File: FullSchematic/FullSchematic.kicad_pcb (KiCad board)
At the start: 4 copper layers, 106 parts, among them J1 USB_A, J10 LCD_Conn, J2 ATX-24, J3 Red Banana Jack, J4 Black Banana Jack, J5 2x6 Pin Header, J6 2x6 Pin Header, J7 CT3151-2, J8 CT3151-2, J9 2x6 Pin Header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

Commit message: Lots of changes with greg
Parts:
- C29, C36, C37, D3, Q3, R21, R22, U10, U11, U12, U13, U14, U9: moved to B.Cu
- moved R15 164.0 mm to (187.5, 70.4)
- moved R19 158.3 mm to (180.7, 68.9)
- moved U8 152.8 mm to (192.8, 79.9)
- moved R16 146.6 mm to (187.5, 65.9)
- moved R20 143.6 mm to (182.8, 65.0)
- moved TP8 138.8 mm to (165.7, 30.1), turned to 90 degrees
- moved TP7 134.1 mm to (162.4, 30.1), turned to 90 degrees
- moved TP6 129.4 mm to (159.0, 30.1), turned to 90 degrees
- moved TP5 124.7 mm to (155.7, 30.1), turned to 90 degrees
- moved TP4 120.0 mm to (152.3, 30.1), turned to 90 degrees
- moved C28 120.0 mm to (98.0, 152.7)
- moved C35 115.5 mm to (98.0, 148.0), turned to 180 degrees
- moved U11 110.4 mm to (106.1, 149.1), turned to 180 degrees
- moved U10 110.0 mm to (106.2, 144.2), turned to 180 degrees
- moved C29 106.9 mm to (82.6, 150.7), turned to 180 degrees
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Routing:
- net COM: track 15.6 -> 154.7 mm, vias 9 -> 82
- net FAULT_N: track 119.7 -> 21.1 mm, vias 1 -> 0
- net OC_RESET_N: track 0.00 -> 47.5 mm
- net Net-(U12-B1): track 0.00 -> 44.3 mm
- net Net-(SW1-4): track 0.00 -> 43.9 mm
- net Net-(U12-B2): track 0.00 -> 43.1 mm
- net Net-(U13-B1): track 0.00 -> 42.4 mm
- net SER: track 0.00 -> 38.4 mm
- net +5V: track 45.3 -> 7.63 mm, vias 0 -> 2
- net *OE: track 0.00 -> 36.7 mm
- net Net-(SW1-2): track 0.00 -> 35.4 mm
- net RCLK: track 0.00 -> 34.2 mm
- net Net-(C6-Pad1): track 0.00 -> 31.5 mm, vias 0 -> 1
- net -5V: track 0.00 -> 31.0 mm, vias 0 -> 1
- net Net-(SW1-8): track 0.00 -> 30.0 mm, vias 0 -> 1
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- added copper zone on B.Cu, net +12V
- added copper zone on In2.Cu, net +12V
- added copper zone on F.Cu, net +5V
- added copper zone on B.Cu, net -12V
- removed copper zone on B.Cu, net (none)
- removed copper zone on F.Cu, net (none)
- removed copper zone on In1.Cu, net COM

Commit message: Semi-complete board
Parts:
- C29, C36, C37, D3, Q3, R21, R22, U10, U11, U12, U13, U14, U9: moved to F.Cu
- J5, J6, J9: footprint Connector_PinHeader_2.54mm:PinHeader_2x06_P2.54mm_Vertical -> CustomFootprints:PMOD
- R11: footprint Resistor_SMD:R_0402_1005Metric -> Resistor_SMD:R_0603_1608Metric
- moved C21 148.0 mm to (220.0, 87.0), turned to -90 degrees
- moved R14 140.2 mm to (199.6, 81.2), turned to -90 degrees
- moved R18 139.9 mm to (214.3, 81.1)
- moved R17 137.6 mm to (214.2, 91.2)
- moved R11 132.5 mm to (214.2, 86.4)
- moved R13 126.7 mm to (196.4, 79.3), turned to -90 degrees
- moved Q2 123.3 mm to (182.2, 79.8)
- moved R12 112.4 mm to (178.4, 82.3), turned to -90 degrees
- moved R10 110.7 mm to (179.4, 78.5), turned to -90 degrees
- moved C19 108.3 mm to (167.6, 151.4)
- moved C20 108.3 mm to (170.8, 156.1)
- moved C22 105.2 mm to (174.6, 151.2)
- moved C30 82.7 mm to (152.1, 153.0)
- moved C31 82.7 mm to (152.1, 156.0)
- moved C32 82.7 mm to (152.1, 159.0)
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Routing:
- net SRCLK: track 0.00 -> 125.2 mm, vias 0 -> 1
- net RCLK: track 34.2 -> 122.8 mm, vias 0 -> 1
- net Net-(U12-B1): track 44.3 -> 127.8 mm
- net Net-(U12-B2): track 43.1 -> 126.3 mm
- net Net-(U13-B1): track 42.4 -> 122.8 mm
- net *OE: track 36.7 -> 115.8 mm
- net SER: track 38.4 -> 113.5 mm
- net C_REF: track 0.00 -> 66.6 mm
- net C_SENSE: track 0.00 -> 53.0 mm, vias 0 -> 1
- net CONTRAST: track 0.20 -> 47.3 mm
- net OC_RESET_N: track 47.5 -> 2.00 mm
- net RELAY_TRIP_N: track 34.1 -> 0.00 mm
- net PWR_ON#: track 0.00 -> 33.5 mm, vias 0 -> 1
- net +5V: track 7.63 -> 38.7 mm, vias 2 -> 6
- net Net-(J10-DB7): track 0.00 -> 19.6 mm
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- added copper zone on B.Cu, net +5V
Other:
- board outline added: 146 x 132 mm

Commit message: PCB V.1
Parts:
- removed C34, C35, C36, C37: .01u, Capacitor_SMD:C_0805_2012Metric
- removed TP1, TP3: TestPoint, TestPoint:TestPoint_2Pads_Pitch2.54mm_Drill0.8mm
- moved TP6 125.1 mm to (128.1, 136.9)
- moved TP8 114.8 mm to (128.1, 115.1)
- moved TP7 98.4 mm to (128.3, 91.2)
- moved C20 86.7 mm to (190.7, 71.7), turned to -90 degrees
- moved TP5 83.1 mm to (128.5, 69.3)
- moved C22 79.3 mm to (180.9, 72.2), turned to -90 degrees
- moved C19 73.3 mm to (199.5, 85.5), turned to -90 degrees
- moved TP4 65.2 mm to (139.3, 34.0)
- moved C25 64.3 mm to (85.3, 139.9), turned to 90 degrees
- moved TP2 62.0 mm to (126.5, 34.5)
- moved C32 60.8 mm to (92.9, 144.9), turned to -90 degrees
- moved C30 51.3 mm to (105.0, 132.6), turned to 90 degrees
- moved C24 48.6 mm to (99.6, 145.4), turned to 180 degrees
- moved C31 48.5 mm to (104.7, 145.3)
- moved C26 43.2 mm to (109.7, 138.2), turned to -90 degrees
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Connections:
- C28 pad 1: +3.3V -> +5V
- C29 pad 1: +3.3V -> +5V
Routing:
- net RELAY_TRIP_N: track 0.00 -> 113.6 mm
- net FAULT_N: track 5.14 -> 86.9 mm, vias 0 -> 1
- net OC_RESET_N: track 2.00 -> 81.8 mm, vias 0 -> 2
- net INV: track 77.4 -> 117.6 mm, vias 2 -> 3
- net NON_INV: track 78.1 -> 114.9 mm, vias 0 -> 1
- net +5V: track 38.7 -> 60.6 mm
- net COM: track 160.7 -> 172.1 mm, vias 86 -> 91
- net Net-(U8-+IN): track 0.00 -> 8.71 mm
- net +3.3V: track 12.3 -> 20.9 mm, vias 6 -> 8
- net C_SENSE: track 53.0 -> 46.3 mm
- net Net-(C20-Pad2): track 0.00 -> 6.36 mm
- net Net-(U4-Gate): track 4.15 -> 9.69 mm
- net Net-(U7-VOUT): track 0.00 -> 3.29 mm
- net Net-(U6-Gate): track 5.42 -> 8.17 mm
- net V_OC: track 2.60 -> 5.21 mm
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- added copper zone on In1.Cu, net COM
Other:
- board text added: "U5"

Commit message: Circuit Board V.2
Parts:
- moved C3 114.1 mm to (180.6, 147.0)
- moved J6 114.1 mm to (167.3, 153.7)
- moved J9 114.1 mm to (141.8, 151.9)
- moved C4 114.1 mm to (194.0, 146.9)
- moved C5 114.1 mm to (193.9, 159.4)
- moved C6 114.1 mm to (180.3, 159.1)
- moved J5 114.1 mm to (154.3, 153.6)
- moved R1 114.1 mm to (180.3, 156.2)
- moved R2 114.1 mm to (193.9, 156.3)
- moved R3 114.1 mm to (194.0, 144.4)
- moved R4 114.1 mm to (180.6, 144.6)
- moved SW1 114.1 mm to (187.4, 152.1)
- moved TP2 114.1 mm to (148.0, 146.6)
- moved TP4 114.1 mm to (160.8, 146.0)
- moved J1 53.9 mm to (46.0, 31.9)
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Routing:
- net Net-(U12-B1): track 127.8 -> 0.00 mm
- net Net-(U12-B2): track 126.3 -> 0.00 mm
- net SRCLK: track 125.2 -> 1.84 mm, vias 1 -> 0
- net Net-(U13-B1): track 122.8 -> 0.00 mm
- net RCLK: track 122.8 -> 1.26 mm, vias 1 -> 0
- net *OE: track 115.8 -> 0.00 mm
- net SER: track 113.5 -> 0.00 mm
- net RELAY_TRIP_N: track 113.6 -> 26.4 mm
- net OC_RESET_N: track 81.8 -> 0.48 mm, vias 2 -> 0
- net NON_INV: track 114.9 -> 64.0 mm, vias 1 -> 0
- net INV: track 117.6 -> 70.5 mm, vias 3 -> 2
- net +5V: track 60.6 -> 27.4 mm, vias 6 -> 3
- net FAULT_N: track 86.9 -> 61.1 mm
- net C_REF: track 64.8 -> 46.7 mm
- net COM: track 172.1 -> 162.0 mm, vias 91 -> 88
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- removed copper zone on B.Cu, net +12V
- removed copper zone on In2.Cu, net +3.3V
- removed copper zone on B.Cu, net +5V
- removed copper zone on F.Cu, net +5V
- removed copper zone on In1.Cu, net COM
- removed copper zone on B.Cu, net Net-(L1-Pad2)
- removed copper zone on F.Cu, net Net-(L1-Pad2)
- removed copper zone on In1.Cu, net Net-(L1-Pad2)
- removed copper zone on In2.Cu, net Net-(L1-Pad2)
- removed copper zone on B.Cu, net Net-(L2-Pad2)
- removed copper zone on F.Cu, net Net-(L2-Pad2)
- removed copper zone on In1.Cu, net Net-(L2-Pad2)
- removed copper zone on In2.Cu, net Net-(L2-Pad2)
- removed copper zone on B.Cu, net Net-(U2-VS)
- removed copper zone on F.Cu, net Net-(U2-VS)
- removed copper zone on In1.Cu, net Net-(U2-VS)
- removed copper zone on In2.Cu, net Net-(U2-VS)
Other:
- board size 146 x 132 mm -> 204 x 151 mm

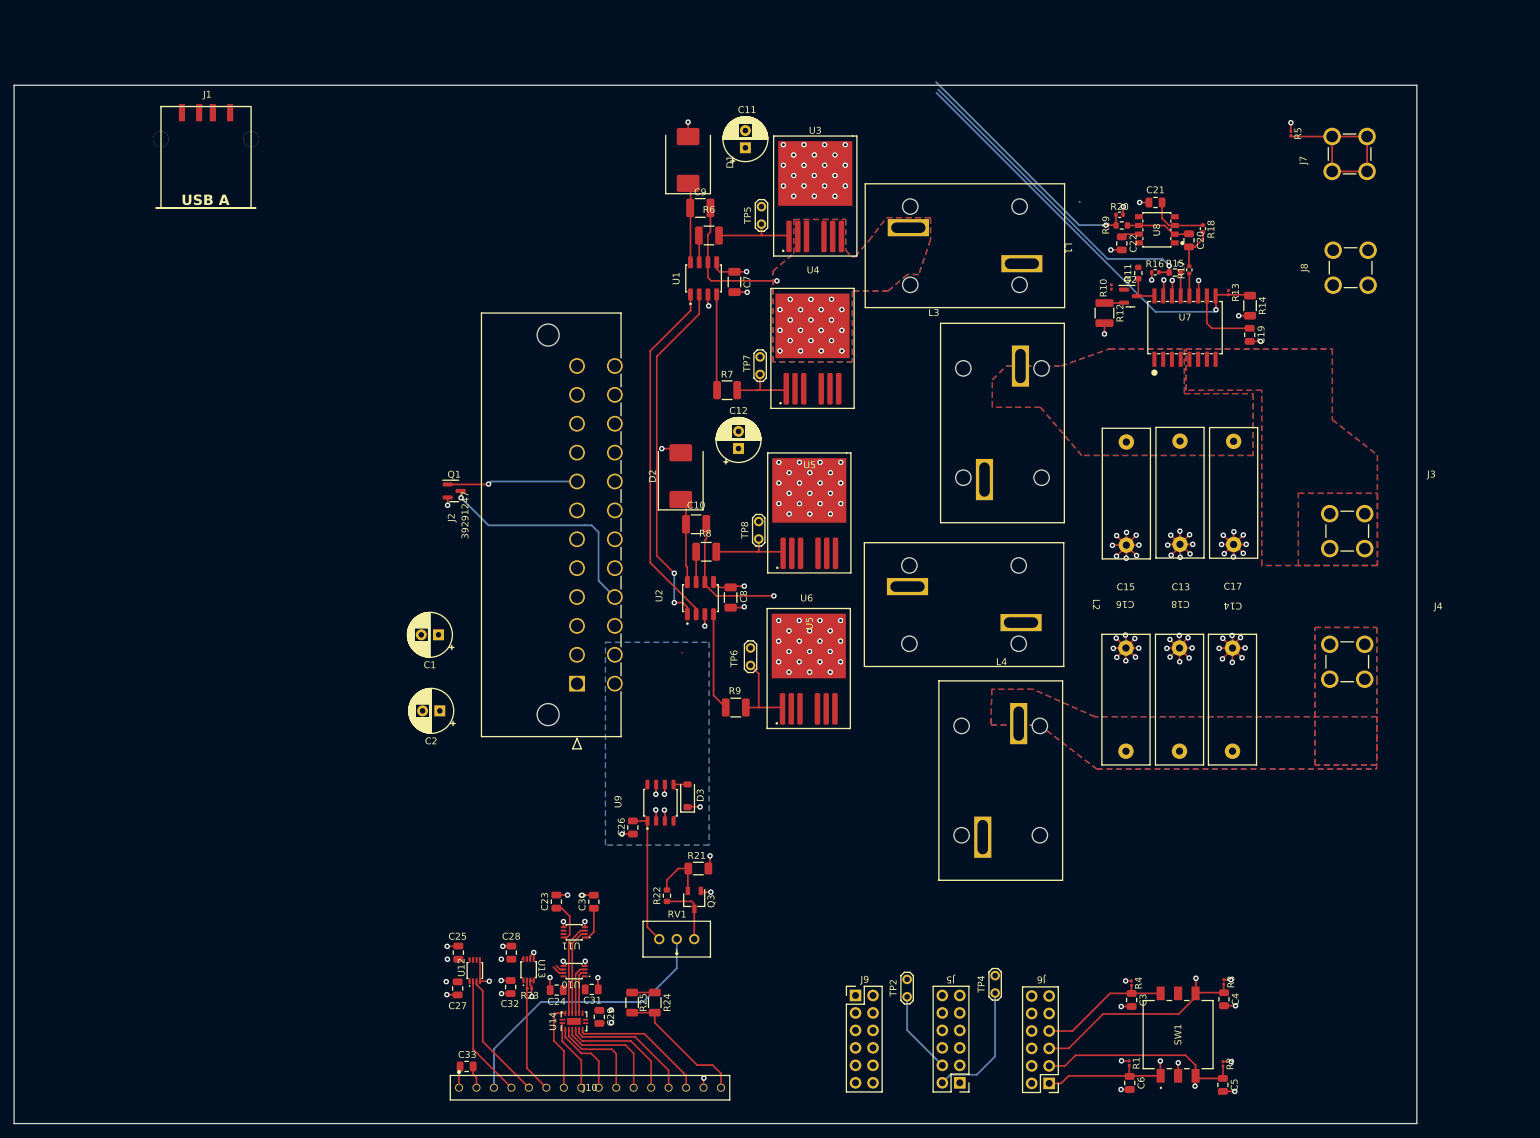
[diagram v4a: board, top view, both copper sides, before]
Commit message: Better LCD layout
Moved LCD to the top of the board, reorganized power planes to be better, more concise locations.
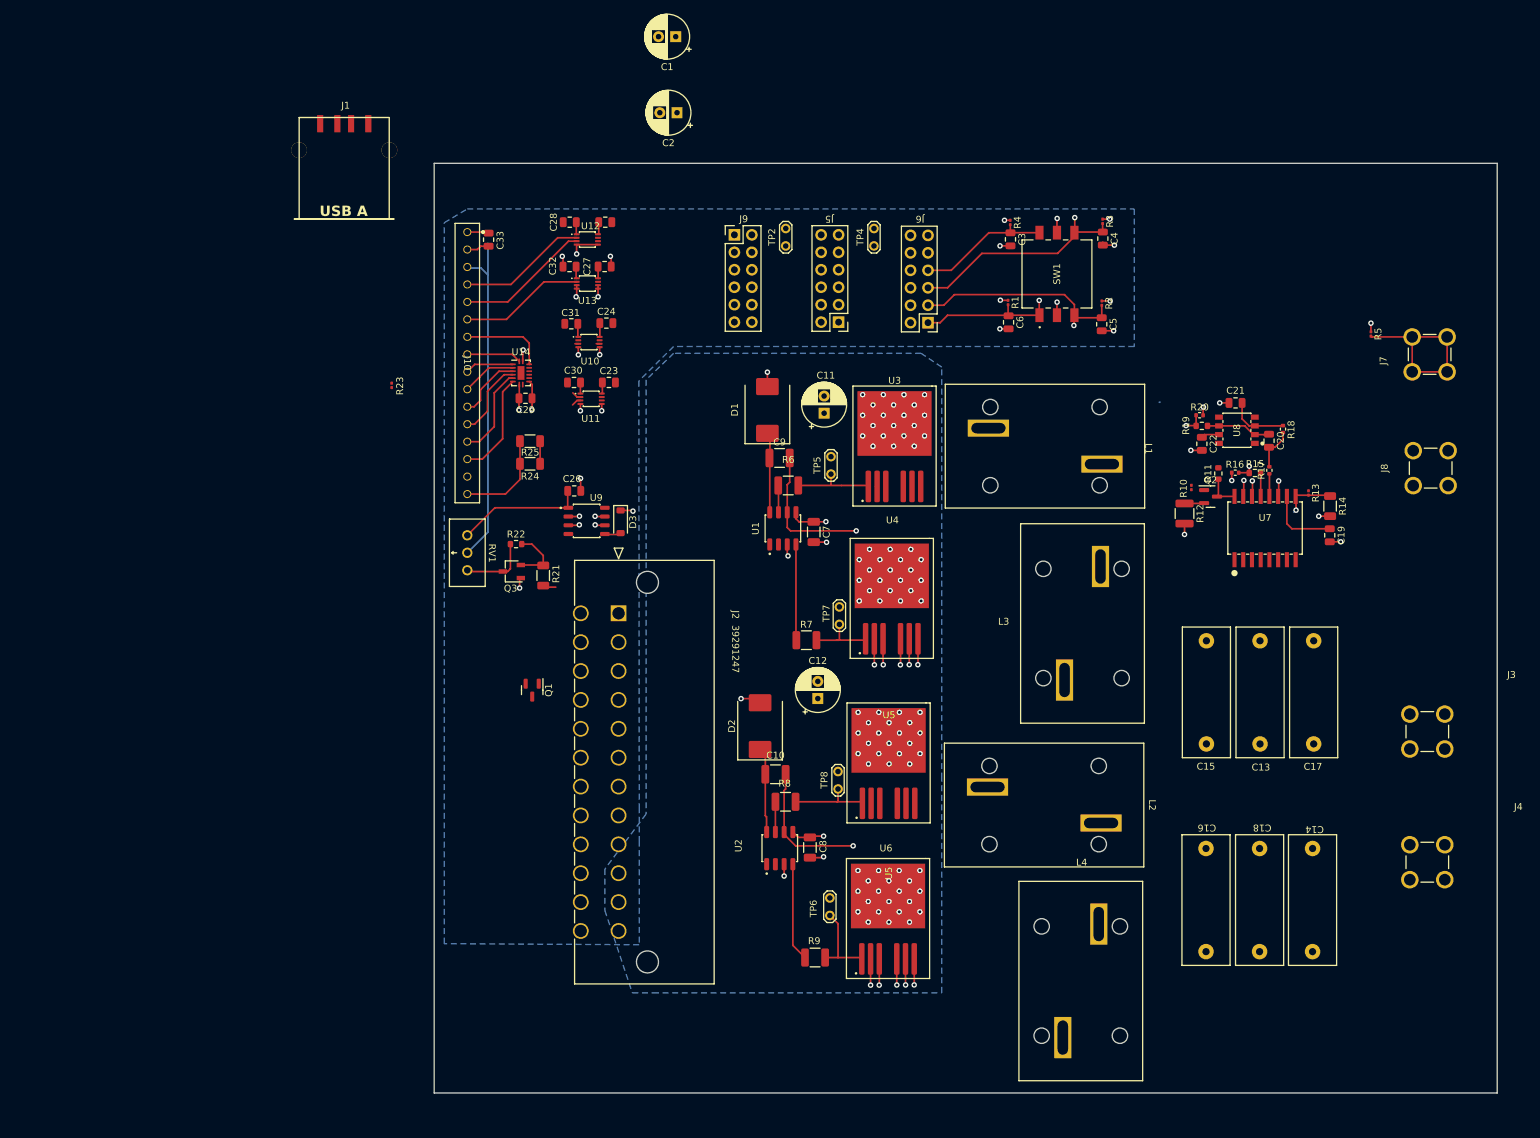
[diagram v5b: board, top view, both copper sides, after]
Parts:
- moved C33 120.3 mm to (87.1, 36.5), turned to 90 degrees
- moved C3 112.0 mm to (163.0, 36.4)
- moved C4 112.0 mm to (176.4, 36.3)
- moved J5 112.0 mm to (136.7, 43.0)
- moved J6 112.0 mm to (149.7, 43.0)
- moved J9 112.0 mm to (124.2, 41.3)
- moved R1 112.0 mm to (162.6, 45.6)
- moved R4 112.0 mm to (163.0, 34.0)
- moved C5 112.0 mm to (176.3, 48.8)
- moved C6 112.0 mm to (162.7, 48.5)
- moved R2 112.0 mm to (176.3, 45.7)
- moved R3 112.0 mm to (176.4, 33.8)
- moved SW1 112.0 mm to (169.8, 41.5)
- moved TP2 110.6 mm to (130.3, 37.4)
- moved TP4 110.1 mm to (143.1, 37.4)
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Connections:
- U14 pad 11: Net-(U10-A1) -> Net-(U11-A2)
- U14 pad 12: Net-(U10-A2) -> Net-(U11-A1)
- U14 pad 13: Net-(U11-A1) -> Net-(U10-A2)
- U14 pad 14: Net-(U11-A2) -> Net-(U10-A1)
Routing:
- net INV: track 70.5 -> 0.40 mm, vias 2 -> 0
- net NON_INV: track 64.0 -> 0.61 mm
- net COM: track 162.0 -> 103.5 mm, vias 88 -> 43
- net FAULT_N: track 61.1 -> 7.59 mm
- net C_REF: track 46.7 -> 2.53 mm
- net PWR_ON#: track 33.5 -> 0.09 mm, vias 1 -> 0
- net C_SENSE: track 36.4 -> 3.05 mm
- net PWR_OK: track 19.5 -> 0.00 mm, vias 1 -> 0
- net Net-(U11-A2): track 13.3 -> 1.40 mm
- net Net-(U11-A1): track 12.6 -> 1.35 mm
- net CONTRAST: track 41.3 -> 49.7 mm
- net Net-(U10-A2): track 7.31 -> 0.49 mm
- net +5V: track 27.4 -> 34.0 mm, vias 3 -> 2
- net Net-(U10-A1): track 6.51 -> 0.00 mm
- net Net-(J10-DB4): track 15.9 -> 9.66 mm
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- added copper zone on B.Cu, net +12V
- added copper zone on B.Cu, net +5V
- removed copper zone on B.Cu, net -12V
- removed copper zone on B.Cu, net AMP_OUT
- removed copper zone on F.Cu, net AMP_OUT
- removed copper zone on In1.Cu, net AMP_OUT
- removed copper zone on In2.Cu, net AMP_OUT
- removed copper zone on B.Cu, net Net-(U1-VS)
- removed copper zone on F.Cu, net Net-(U1-VS)
- removed copper zone on In1.Cu, net Net-(U1-VS)
- removed copper zone on In2.Cu, net Net-(U1-VS)
- removed copper zone on B.Cu, net OCTA_IN
- removed copper zone on F.Cu, net OCTA_IN
- removed copper zone on In1.Cu, net OCTA_IN
- removed copper zone on In2.Cu, net OCTA_IN
- removed copper zone on B.Cu, net OCTA_OUT
- removed copper zone on F.Cu, net OCTA_OUT
- removed copper zone on In1.Cu, net OCTA_OUT
- removed copper zone on In2.Cu, net OCTA_OUT
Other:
- board size 204 x 151 mm -> 154.6 x 135.2 mm
